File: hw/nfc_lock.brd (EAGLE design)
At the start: 68.2 x 90.2 mm, 37 parts, among them IC1 STM8S003F3, IC3 MCP170312MB, Q1 8MHz, Q3 2N7002,215, U1 M24SR16-YMN6T/2, U2 2N7002,215, U3 2N7002,215, U4 IRFML8244TRPBF, X1 MINI-USB-32005-301

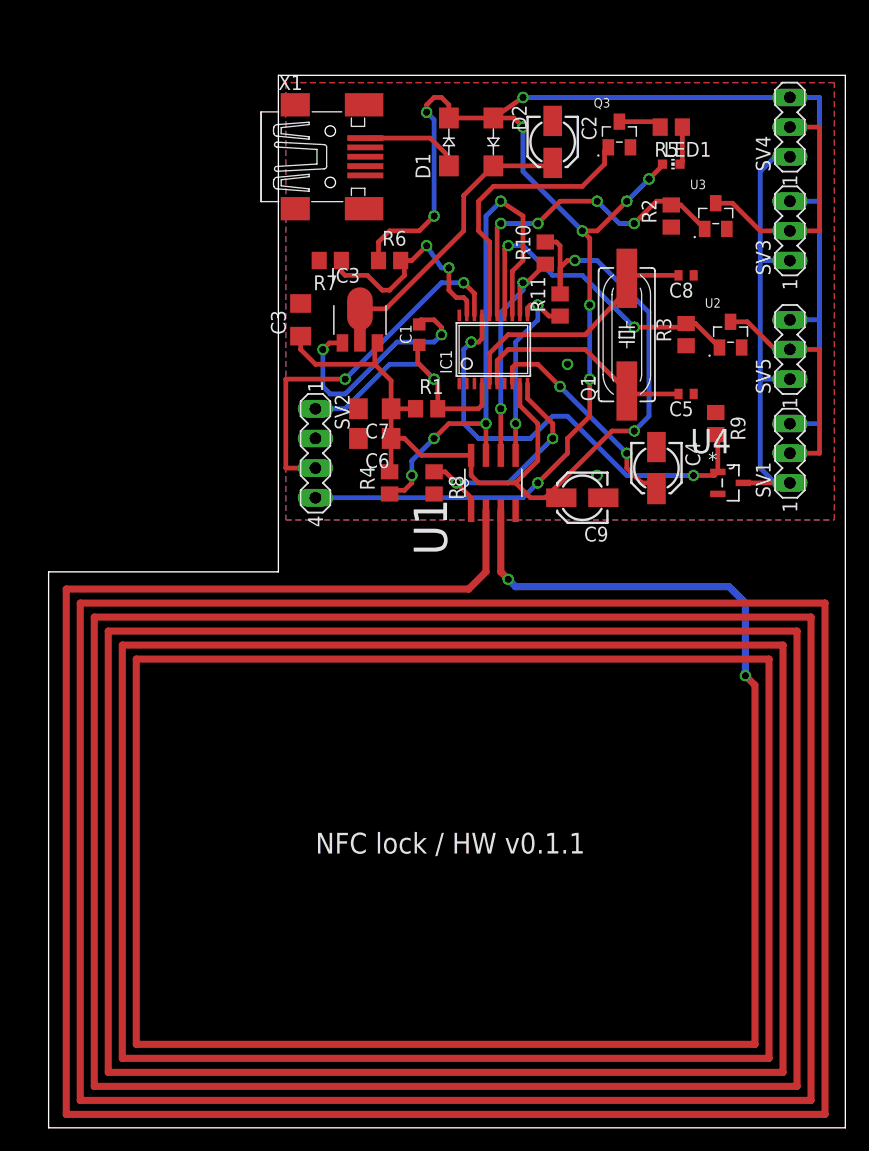
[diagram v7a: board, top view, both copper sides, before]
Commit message: additional 4.7uF for general power decoupling
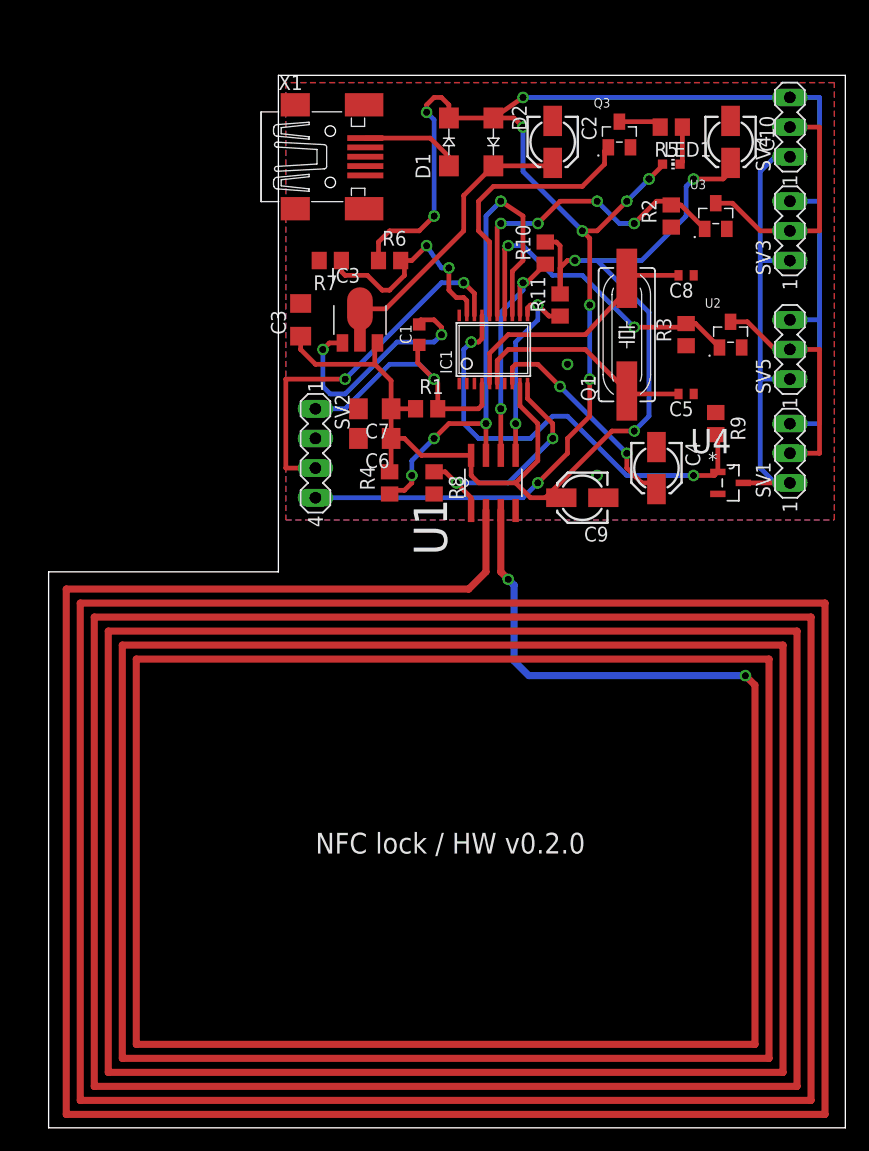
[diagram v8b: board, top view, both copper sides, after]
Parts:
- added C10: 4.7uF, rcl:153CLV-0405
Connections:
- net +5V/1: now also C10.+
- net 0V: now also C10.-
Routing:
- net +5V/1: track 87.7 -> 104.5 mm, vias 2 -> 3
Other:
- board text added: "NFC lock / HW v0.2.0"
- board text removed: "NFC lock / HW v0.1.1"
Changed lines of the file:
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@@
 <wire x1="26.035" y1="34.29" x2="6.35" y2="34.29" width="0" layer="20"/>
 <wire x1="6.35" y1="34.29" x2="6.35" y2="-13.335" width="0" layer="20"/>
-<text x="29.21" y="10.16" size="1.778" layer="25">NFC lock / HW v0.1.1</text>
+<text x="29.21" y="10.16" size="1.778" layer="25">NFC lock / HW v0.2.0</text>
 </plain>
 <attributes>
@@
 <element name="R10" library="rcl" package="R0805" value="4.7k" x="48.895" y="61.595" rot="R90"/>
 <element name="R11" library="rcl" package="R0805" value="4.7k" x="50.165" y="57.15" rot="R90"/>
+<element name="C10" library="rcl" package="153CLV-0405" value="4.7uF" x="64.77" y="71.12" rot="R270"/>
 </elements>
 <signals>
@@
 <contactref element="C7" pad="2"/>
 <contactref element="C9" pad="-"/>
+<contactref element="C10" pad="-"/>
 </signal>
 <signal name="+5V/1">
@@
 <wire x1="35.69" y1="48.26" x2="35.69" y2="50.67" width="0.4064" layer="1"/>
 <wire x1="35.69" y1="50.67" x2="34.29" y2="52.07" width="0.4064" layer="1"/>
+<contactref element="C10" pad="+"/>
+<wire x1="53.34" y1="60.96" x2="57.15" y2="60.96" width="0.4064" layer="16"/>
+<wire x1="57.15" y1="60.96" x2="60.96" y2="64.77" width="0.4064" layer="16"/>
+<wire x1="60.96" y1="64.77" x2="60.96" y2="67.31" width="0.4064" layer="16"/>
+<wire x1="60.96" y1="67.31" x2="61.595" y2="67.945" width="0.4064" layer="16"/>
+<via x="61.595" y="67.945" extent="1-16" drill="0.6"/>
+<wire x1="61.595" y1="67.945" x2="64.135" y2="67.945" width="0.4064" layer="1"/>
+<wire x1="64.135" y1="67.945" x2="64.77" y2="68.58" width="0.4064" layer="1"/>
+<wire x1="64.77" y1="68.58" x2="64.77" y2="69.32" width="0.4064" layer="1"/>
 </signal>
 <signal name="+5V">
@@
 <wire x1="45.085" y1="34.29" x2="45.72" y2="33.655" width="0.6096" layer="1"/>
 <via x="45.72" y="33.655" extent="1-16" drill="0.6"/>
-<wire x1="45.72" y1="33.655" x2="46.355" y2="33.02" width="0.6096" layer="16"/>
-<wire x1="46.355" y1="33.02" x2="64.63538125" y2="33.02" width="0.6096" layer="16"/>
-<wire x1="64.63538125" y1="33.02" x2="66.04" y2="31.61538125" width="0.6096" layer="16"/>
-<wire x1="66.04" y1="31.61538125" x2="66.04" y2="25.4" width="0.6096" layer="16"/>
 <wire x1="66.86041875" y1="24.5999" x2="66.8401" y2="24.5999" width="0.4064" layer="1"/>
 <wire x1="66.8401" y1="24.5999" x2="66.04" y2="25.4" width="0.6096" layer="1"/>
+<wire x1="46.22038125" y1="26.67" x2="46.22038125" y2="33.15461875" width="0.6096" layer="16"/>
+<wire x1="46.22038125" y1="33.15461875" x2="45.72" y2="33.655" width="0.6096" layer="16"/>
+<wire x1="66.04" y1="25.4" x2="47.49038125" y2="25.4" width="0.6096" layer="16"/>
+<wire x1="47.49038125" y1="25.4" x2="46.22038125" y2="26.67" width="0.6096" layer="16"/>
 </signal>
 <signal name="SERVO_PACK_2">
